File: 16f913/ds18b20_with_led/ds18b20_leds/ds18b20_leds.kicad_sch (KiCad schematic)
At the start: 39 parts, among them J1 MTA06-156, Q1 20.0MHz, T1 BC337, T2 BC337, T3 BC337, T4 BC337, T5 BC337, U1 CC56-12EWA, U2 HDSP-7501, U3 PIC16F913-XXISP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

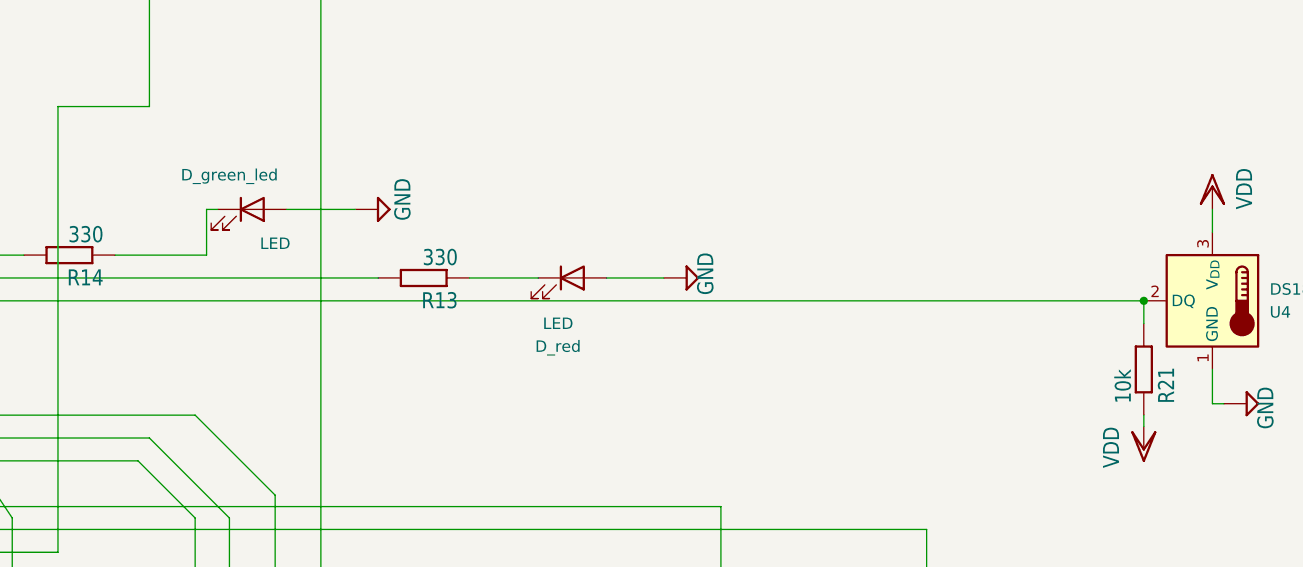
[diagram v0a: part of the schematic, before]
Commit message: test of ds18b20 updated tested for 4 sensors
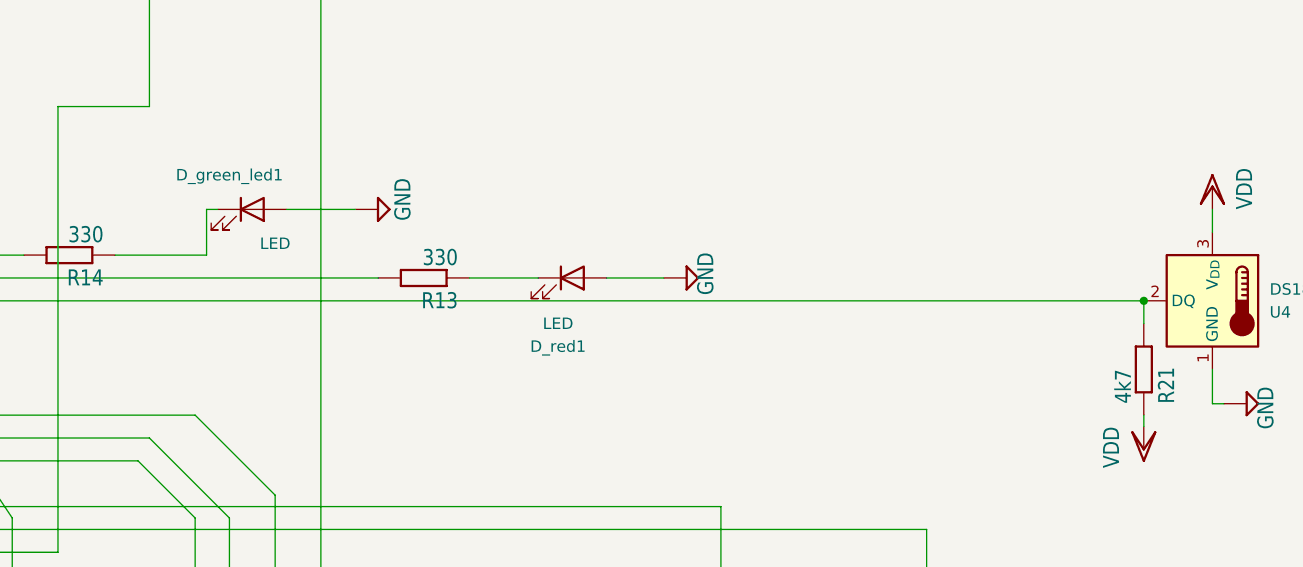
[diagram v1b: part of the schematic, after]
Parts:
- R21: value 10k -> 4k7
- renumbered D_green_led to D_green_led1, D_red to D_red1
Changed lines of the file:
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@@
 			)
 		)
-		(property "Value" "10k"
+		(property "Value" "4k7"
 			(at 298.958 139.7 0)
 			(effects
@@
 		(on_board yes)
 		(dnp no)
-		(property "Reference" "D_green_led"
+		(property "Reference" "D_green_led1"
 			(at 200.66 114.3 0)
 			(effects
@@
 			(project ""
 				(path "/841da6f7-1698-4810-a4eb-50d82cc331bc"
-					(reference "D_green_led")
+					(reference "D_green_led1")
 					(unit 1)
 				)
@@
 		(dnp no)
 		(fields_autoplaced yes)
-		(property "Reference" "D_red"
+		(property "Reference" "D_red1"
 			(at 237.1725 133.35 0)
 			(effects
@@
 			(project ""
 				(path "/841da6f7-1698-4810-a4eb-50d82cc331bc"
-					(reference "D_red")
-					(unit 1)
-				)
+					(reference "D_red1")
+					(unit 1)
+				)
